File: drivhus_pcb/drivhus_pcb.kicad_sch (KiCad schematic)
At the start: 4 parts

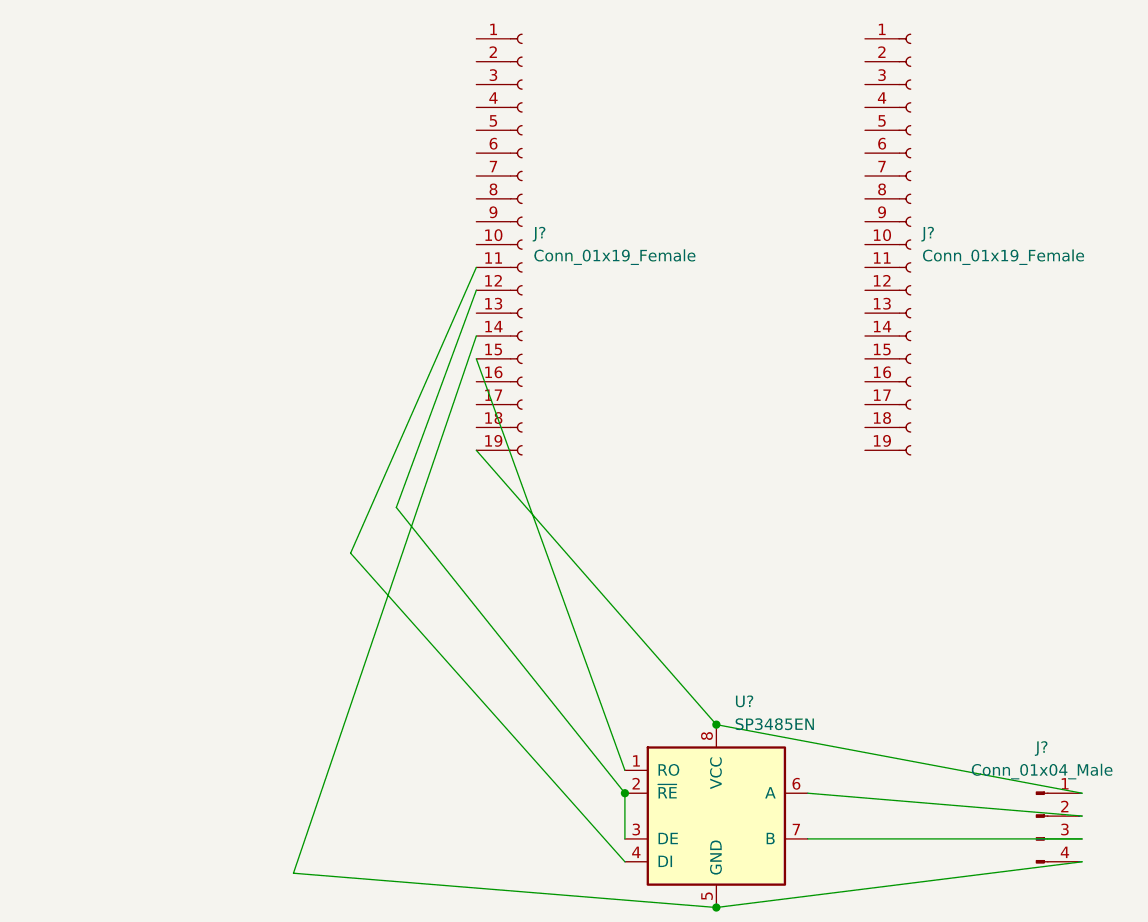
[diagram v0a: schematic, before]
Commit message: Added stup mode jumper to schematics
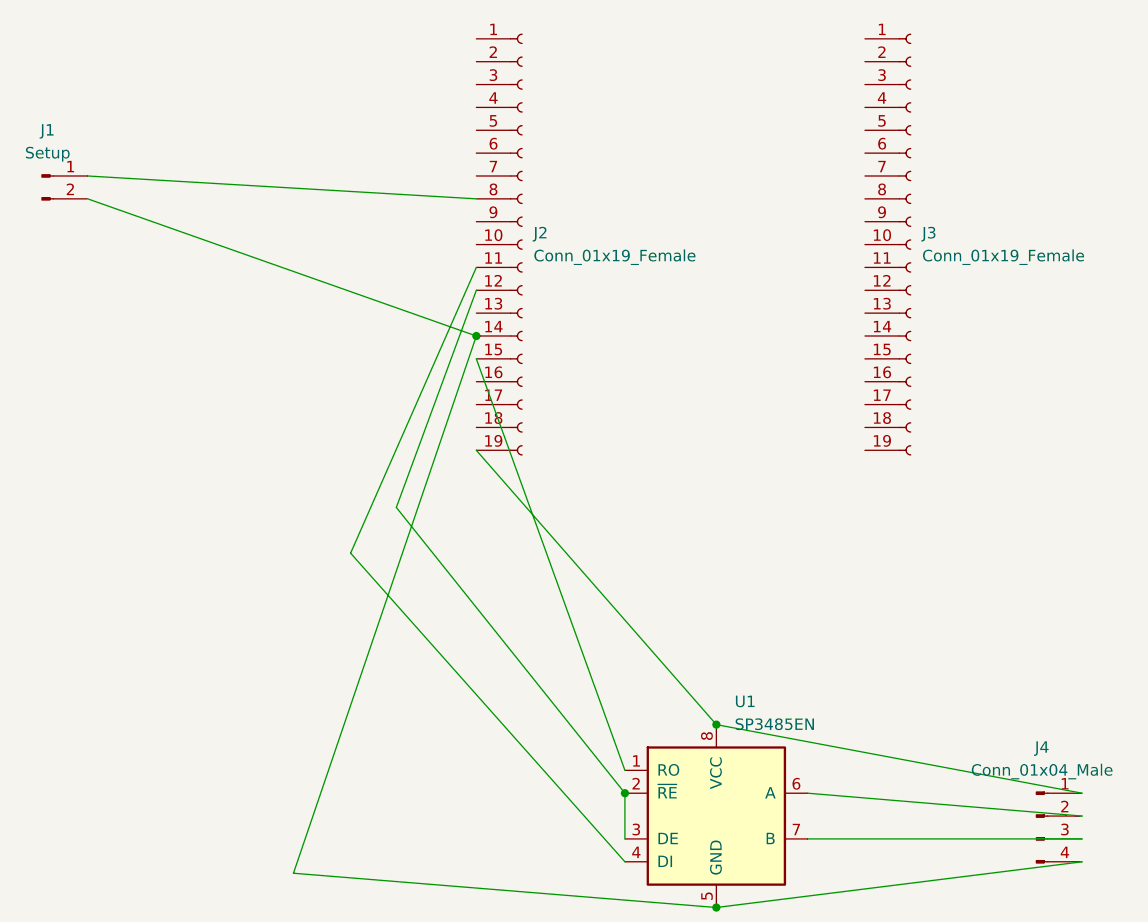
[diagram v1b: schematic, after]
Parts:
- added J1: Setup, symbol Connector:Conn_01x02_Male
- gave numbers to parts that had none: 4
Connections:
- net at J2.14 (Pin_14), J4.4 (Pin_4), U1.5 (GND): now also J1.2 (Pin_2)
- net at J2.8 (Pin_8): now also J1.1 (Pin_1)
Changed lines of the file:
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@@
   (junction (at 115.57 146.05) (diameter 0) (color 0 0 0 0)
+  )
+  (junction (at 99.06 95.25) (diameter 0) (color 0 0 0 0)
   )
   (wire (pts (xy 78.74 154.94) (xy 125.73 158.75))
@@
     (stroke (width 0) (type default) (color 0 0 0 0))
   )
+  (wire (pts (xy 99.06 95.25) (xy 55.88 80.01))
+    (stroke (width 0) (type default) (color 0 0 0 0))
+  )
   (wire (pts (xy 135.89 151.13) (xy 166.37 151.13))
     (stroke (width 0) (type default) (color 0 0 0 0))
@@
     (stroke (width 0) (type default) (color 0 0 0 0))
   )
+  (wire (pts (xy 99.06 80.01) (xy 55.88 77.47))
+    (stroke (width 0) (type default) (color 0 0 0 0))
+  )
   (symbol (lib_id "Connector:Conn_01x19_Female") (at 104.14 85.09 0) (unit 1)
     (in_bom yes) (on_board yes) (fields_autoplaced)
-    (property "Reference" "J?" (id 0) (at 105.41 83.8199 0)
+    (property "Reference" "J2" (id 0) (at 105.41 83.8199 0)
       (effects (font (size 1.27 1.27)) (justify left))
     )
@@
   (symbol (lib_id "Connector:Conn_01x19_Female") (at 147.32 85.09 0) (unit 1)
     (in_bom yes) (on_board yes) (fields_autoplaced)
-    (property "Reference" "J?" (id 0) (at 148.59 83.8199 0)
+    (property "Reference" "J3" (id 0) (at 148.59 83.8199 0)
       (effects (font (size 1.27 1.27)) (justify left))
     )
@@
   (symbol (lib_id "Connector:Conn_01x04_Male") (at 161.29 148.59 0) (unit 1)
     (in_bom yes) (on_board yes) (fields_autoplaced)
-    (property "Reference" "J?" (id 0) (at 161.925 140.97 0))
+    (property "Reference" "J4" (id 0) (at 161.925 140.97 0))
     (property "Value" "Conn_01x04_Male" (id 1) (at 161.925 143.51 0))
     (property "Footprint" "" (id 2) (at 161.29 148.59 0)
@@
   (symbol (lib_id "Interface_UART:SP3485EN") (at 125.73 148.59 0) (unit 1)
     (in_bom yes) (on_board yes) (fields_autoplaced)
-    (property "Reference" "U?" (id 0) (at 127.7494 135.89 0)
+    (property "Reference" "U1" (id 0) (at 127.7494 135.89 0)
       (effects (font (size 1.27 1.27)) (justify left))
     )
@@
     (pin "8")
   )
+  (symbol (lib_id "Connector:Conn_01x02_Male") (at 50.8 77.47 0) (unit 1)
+    (in_bom yes) (on_board yes) (fields_autoplaced)
+    (property "Reference" "J1" (id 0) (at 51.435 72.39 0))
+    (property "Value" "Setup" (id 1) (at 51.435 74.93 0))
+    (property "Footprint" "" (id 2) (at 50.8 77.47 0)
+      (effects (font (size 1.27 1.27)) hide)
+    )
+    (property "Datasheet" "~" (id 3) (at 50.8 77.47 0)
+      (effects (font (size 1.27 1.27)) hide)
+    )
+    (pin "1")
+    (pin "2")
+  )
   (sheet_instances
     (path "/" (page "1"))
   )
   (symbol_instances
+    (path "/cc1d9e72-6d7e-4b1a-895f-9e83cfa7ed74"
+      (reference "J1") (unit 1) (value "Setup") (footprint "")
+    )
     (path "/2d5cde52-f66b-4d74-a993-25971513d148"
-      (reference "J?") (unit 1) (value "Conn_01x19_Female") (footprint "")
+      (reference "J2") (unit 1) (value "Conn_01x19_Female") (footprint "")
     )
     (path "/706786b0-5686-45a1-ae8f-15f99e917918"
-      (reference "J?") (unit 1) (value "Conn_01x19_Female") (footprint "")
+      (reference "J3") (unit 1) (value "Conn_01x19_Female") (footprint "")
     )
     (path "/76df43cb-8047-4fdb-b097-721514b7aec0"
-      (reference "J?") (unit 1) (value "Conn_01x04_Male") (footprint "")
+      (reference "J4") (unit 1) (value "Conn_01x04_Male") (footprint "")
     )
     (path "/ba1d673c-507b-434f-9d3f-83c44effc345"
-      (reference "U?") (unit 1) (value "SP3485EN") (footprint "Package_SO:SOIC-8_3.9x4.9mm_P1.27mm")
+      (reference "U1") (unit 1) (value "SP3485EN") (footprint "Package_SO:SOIC-8_3.9x4.9mm_P1.27mm")
     )
   )

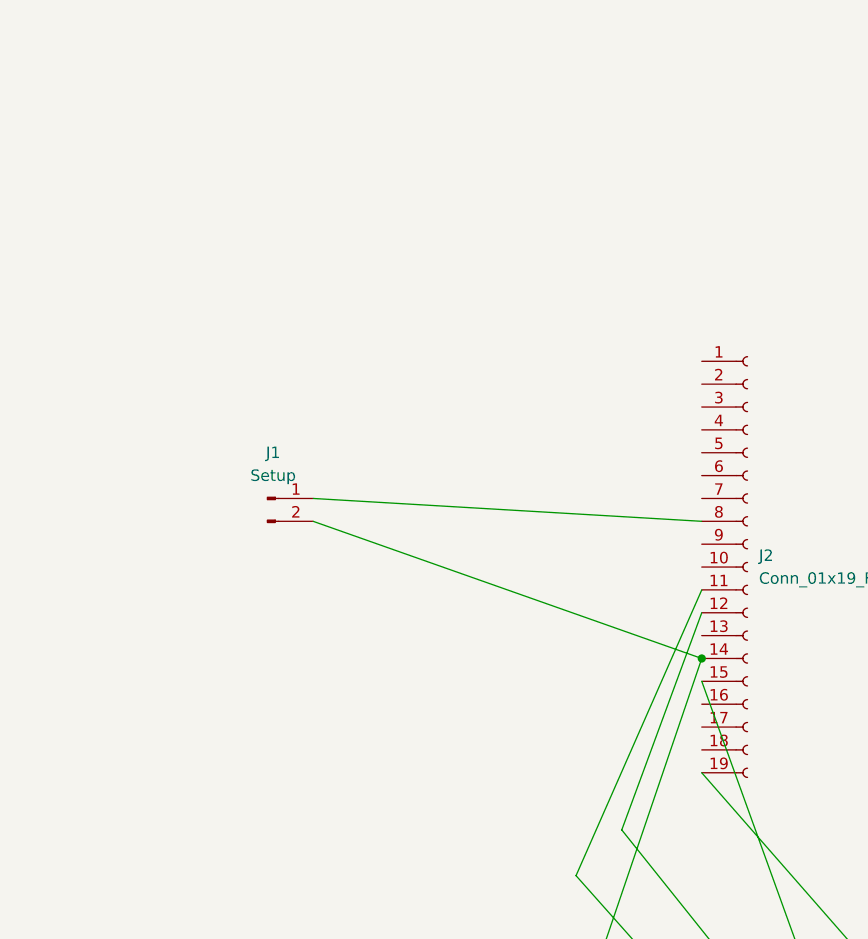
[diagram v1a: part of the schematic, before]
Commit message: Added pins for the DC-DC power
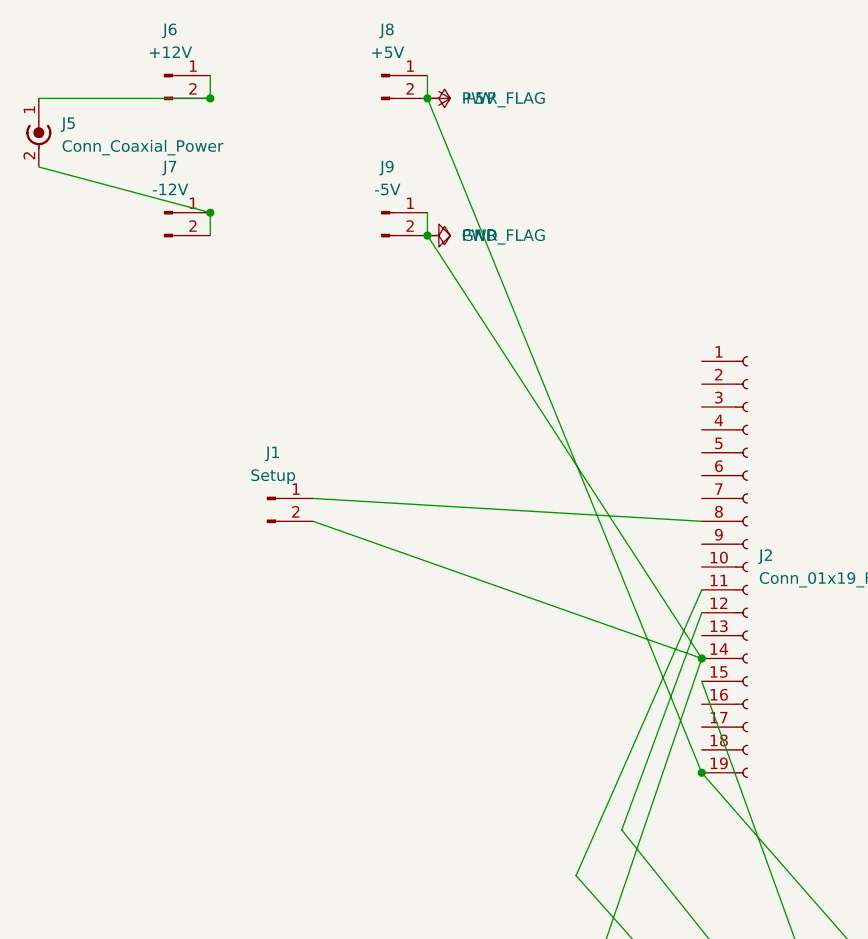
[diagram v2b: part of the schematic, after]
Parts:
- added J5: Conn_Coaxial_Power, CustomLibrary:BarrelJack_Wuerth_6941xx301002, symbol Connector:Conn_Coaxial_Power
- added J6: +12V, Connector_PinHeader_2.54mm:PinHeader_1x02_P2.54mm_Vertical, symbol Connector:Conn_01x02_Male
- added J7: -12V, Connector_PinHeader_2.54mm:PinHeader_1x02_P2.54mm_Vertical, symbol Connector:Conn_01x02_Male
- added J8: +5V, Connector_PinHeader_2.54mm:PinHeader_1x02_P2.54mm_Vertical, symbol Connector:Conn_01x02_Male
- added J9: -5V, Connector_PinHeader_2.54mm:PinHeader_1x02_P2.54mm_Vertical, symbol Connector:Conn_01x02_Male
- J1: footprint (none) -> Connector_PinHeader_2.54mm:PinHeader_1x02_P2.54mm_Vertical
- J2, J3: footprint (none) -> Connector_PinHeader_2.54mm:PinHeader_1x19_P2.54mm_Vertical
- J4: footprint (none) -> TerminalBlock:TerminalBlock_bornier-4_P5.08mm
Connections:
- net GND: now reaches J1.2 (Pin_2), J2.14 (Pin_14), J4.4 (Pin_4), U1.5 (GND)
- net GND: now also J9.1 (Pin_1), J9.2 (Pin_2)
- net +5V: now reaches J2.19 (Pin_19), J4.1 (Pin_1), U1.8 (VCC)
- net +5V: now also J8.1 (Pin_1), J8.2 (Pin_2)
- new net: J5.1 (In), J6.1 (Pin_1), J6.2 (Pin_2)
- new net: J5.2 (Ext), J7.1 (Pin_1), J7.2 (Pin_2)
